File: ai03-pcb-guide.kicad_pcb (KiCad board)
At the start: 2 copper layers, 24 parts, among them SW1 SW_Push, U1 ATmega32U4-AU, Y1 Crystal_GND24_Small

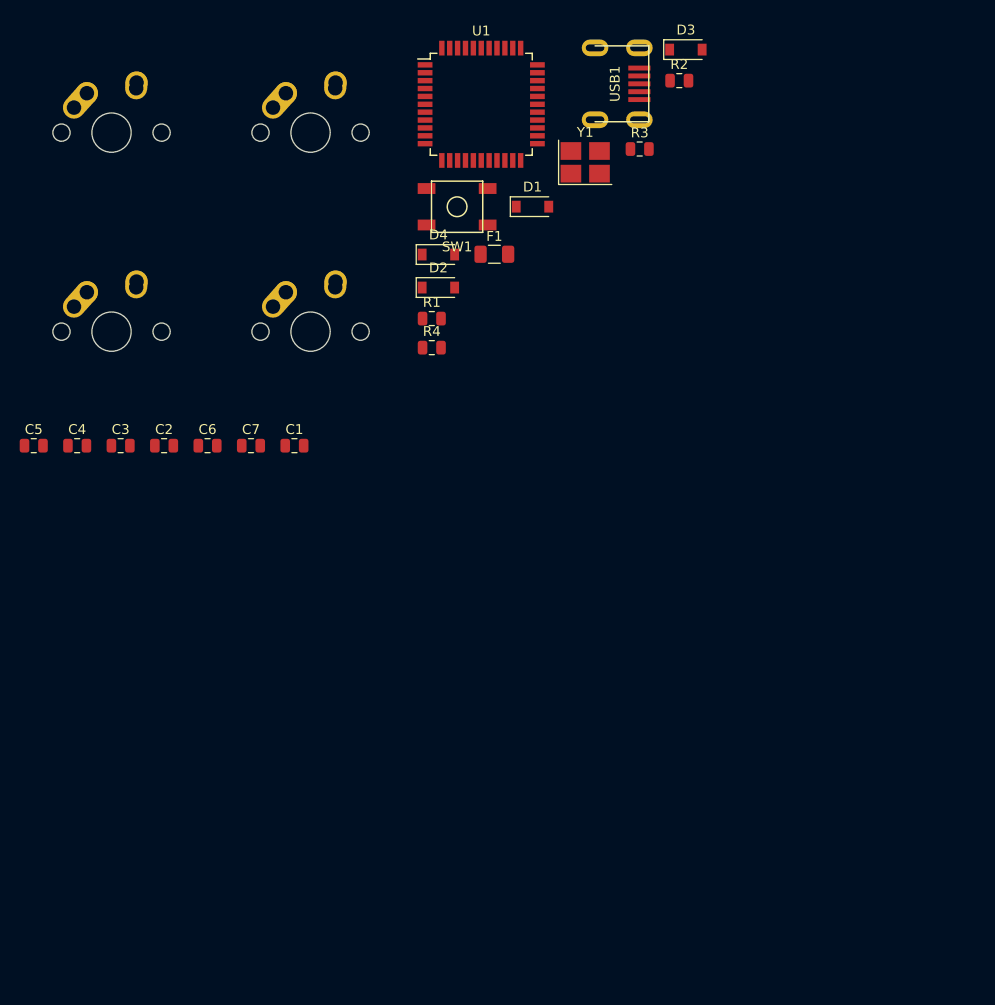
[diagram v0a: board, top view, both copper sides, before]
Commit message: components placed
components placed in their place and routed correctly.
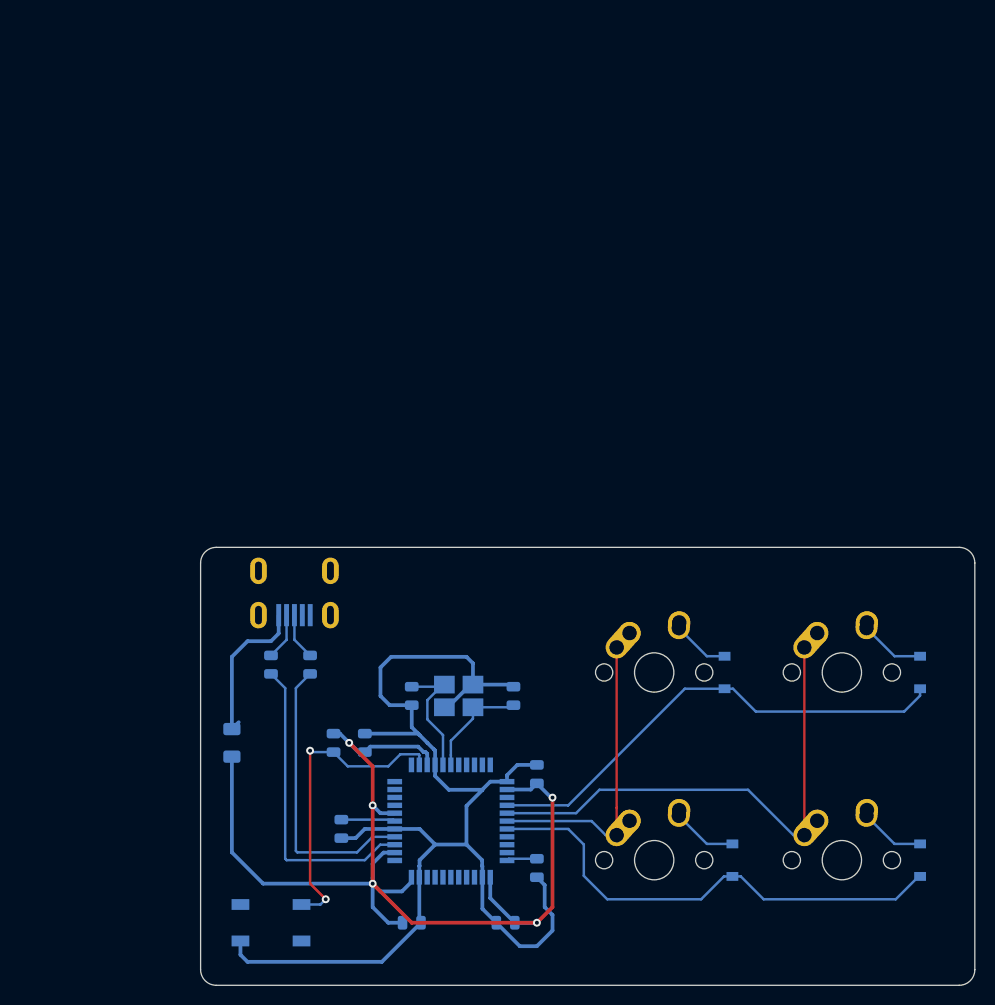
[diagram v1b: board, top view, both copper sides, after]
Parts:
- C1, C2, C3, C4, C5, C6, C7, D1, D2, D3, D4, F1, R1, R2, R3, R4, SW1, U1, USB1, Y1: moved to B.Cu
- moved MX2 92.1 mm to (87.3, 103.2)
- moved D4 78.5 mm to (114.3, 103.2), turned to 90 degrees
- moved MX3 76.9 mm to (106.4, 84.1)
- moved MX4 76.1 mm to (106.4, 103.2)
- moved SW1 75.1 mm to (48.4, 109.5), turned to 180 degrees
- moved U1 72.8 mm to (66.7, 99.2)
- moved R2 70.1 mm to (52.4, 83.3), turned to 90 degrees
- moved D1 69.4 mm to (95.2, 103.2), turned to 90 degrees
- moved R3 67.8 mm to (54.8, 91.3), turned to 90 degrees
- moved D3 67.5 mm to (114.3, 84.1), turned to 90 degrees
- moved MX1 65.0 mm to (87.3, 84.1)
- moved C5 61.0 mm to (75.4, 94.5), turned to 90 degrees
- moved C2 59.5 mm to (72.2, 109.5), turned to 180 degrees
- moved USB1 58.1 mm to (50.8, 73.8), turned to 270 degrees
- moved F1 56.3 mm to (44.5, 91.3), turned to 90 degrees
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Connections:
- U1 pad 26: Net-(U1-Pad26) -> ROW0
- U1 pad 27: Net-(U1-Pad27) -> COL1
- U1 pad 28: Net-(U1-Pad28) -> COL0
- U1 pad 29: Net-(U1-Pad29) -> ROW1
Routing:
- net GND: track 0.00 -> 126.0 mm
- net +5V: track 0.00 -> 116.1 mm, vias 0 -> 5
- net COL1: track 0.00 -> 52.1 mm
- net ROW1: track 0.00 -> 49.6 mm
- net ROW0: track 0.00 -> 49.2 mm
- net Net-(R3-Pad1): track 0.00 -> 31.7 mm, vias 0 -> 2
- net Net-(R1-Pad1): track 0.00 -> 31.2 mm
- net COL0: track 0.00 -> 30.8 mm
- net Net-(R2-Pad1): track 0.00 -> 29.3 mm
- net VCC: track 0.00 -> 15.9 mm
- net Net-(C4-Pad2): track 0.00 -> 13.3 mm
- net Net-(C3-Pad1): track 0.00 -> 11.0 mm
- net Net-(D1-Pad2): track 0.00 -> 6.62 mm
- net Net-(D4-Pad2): track 0.00 -> 6.62 mm
- net Net-(D3-Pad2): track 0.00 -> 6.62 mm
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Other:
- board outline added: 78.6 x 44.5 mm
- net class Default: trace_width 0.25 -> 0.254
- net class Power added: clearance 0.2, trace_width 0.381, via_dia 0.8, via_drill 0.4

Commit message: test complete, gerber file created
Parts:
- moved USB1 0.79 mm to (50.8, 73.0)
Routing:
- added copper zone on B.Cu, net GND
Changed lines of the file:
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@@
   )
   (module random-keyboard-parts:Molex-0548190589 (layer B.Cu)
-    (at 50.8 73.81875 270)
+    (at 50.8 73.025 270)
     (attr smd)
     (fp_text reference USB1 (at 2.032 0) (layer B.SilkS)
@@
   (segment (start 72.55 103.04375) (end 72.375 103.21875) (width 0.254) (layer B.Cu) (net 20))
   (segment (start 75.40625 103.04375) (end 72.55 103.04375) (width 0.254) (layer B.Cu) (net 20))
+  (zone (net 1) (net_name GND) (layer B.Cu) (hatch edge 0.508)
+    (connect_pads (clearance 0.508))
+    (min_thickness 0.254)
+    (fill yes (arc_segments 32) (thermal_gap 0.508) (thermal_bridge_width 0.508))
+    (polygon
+      (pts
+        (xy 41.275 71.4375) (xy 77.7875 71.4375) (xy 77.7875 115.8875) (xy 41.275 115.8875)
+      )
+    )
+  )
 )
